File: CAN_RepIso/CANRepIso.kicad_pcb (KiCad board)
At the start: 4 copper layers, 57 x 27 mm, 82 parts, among them U1 SN74LV32ADGVR, U10 AP2205-33W5-7, U11 AP2205-33W5-7, U2 SN74LVC2G08DCUR, U3 SN74LVC2G07DBVR, U4 SN74LVC2G04DBVR, U5 SN74LVC2G132DCUR, U6 SN65HVD230, U7 PLACEHOLDER ISOLATOR, U8 SN65HVD230, U9 ADuM120N

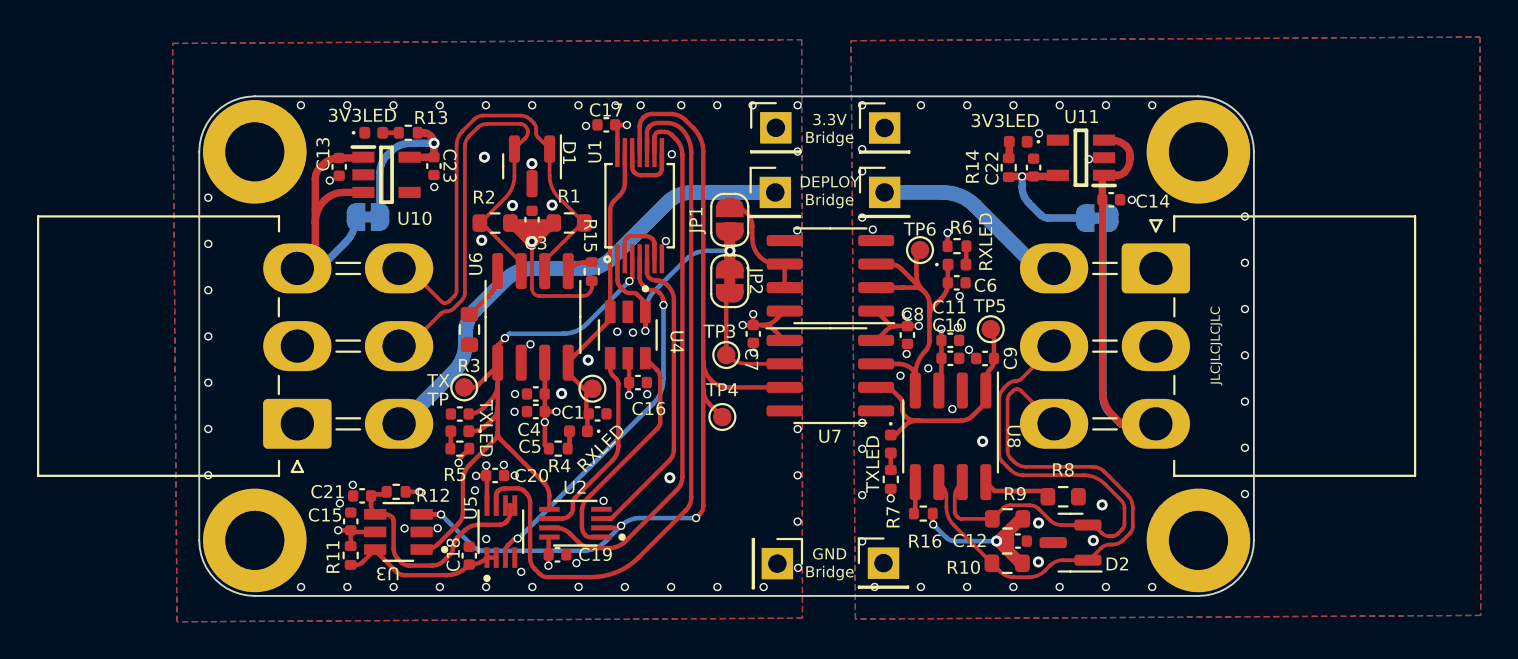
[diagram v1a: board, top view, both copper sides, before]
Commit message: clean up schematic and bom
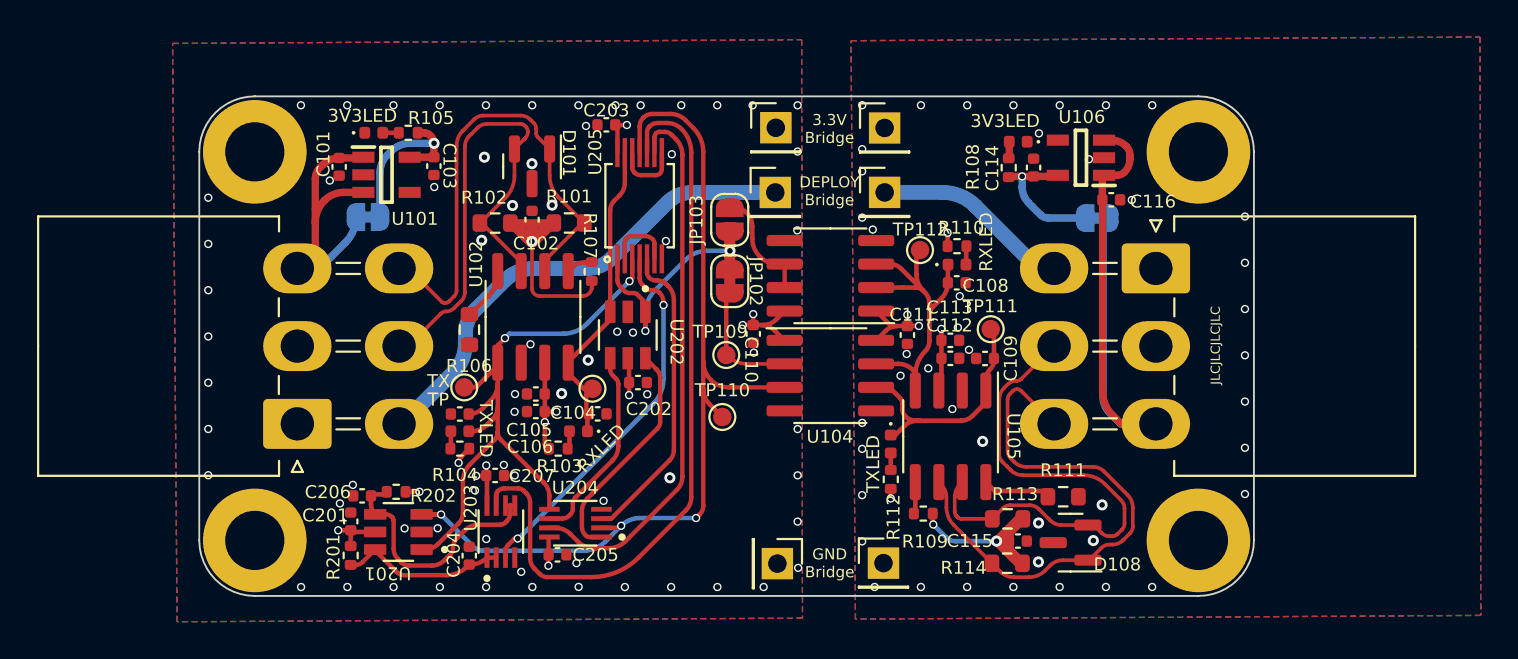
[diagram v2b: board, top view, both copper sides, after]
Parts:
- C201: renamed from C15; value 0.1uF -> 100nF
- C202: renamed from C16; value 0.1uF -> 100nF
- C203: renamed from C17; value 0.1uF -> 100nF
- C205: renamed from C19; value 0.1uF -> 100nF
- C207: renamed from C20; value 0.1uF -> 100nF
- D102: renamed from D3; value RX1LED -> LED_ORANGE
- D103: renamed from D4; value TX1LED -> LED_GREEN
- D104: renamed from D7; value 3V31LED -> LED_BLUE
- D105: renamed from D8; value 3V32LED -> LED_BLUE
- D106: renamed from D5; value RX2LED -> LED_ORANGE
- D107: renamed from D6; value TX2LED -> LED_GREEN
- renumbered C13 to C101, C3 to C102, C23 to C103, C1 to C104, C4 to C105, C5 to C106, C2 to C107, C6 to C108, C9 to C109, C7 to C110, C8 to C111, C10 to C112, C11 to C113, C22 to C114, C12 to C115, C14 to C116, C18 to C204, C21 to C206, D1 to D101, D2 to D108, H1 to H101, H2 to H102, H3 to H103, H4 to H104, RBUS1 to J101, RBUS2 to J102, JP4 to JP101, JP2 to JP102, JP1 to JP103, JP3 to JP104, R1 to R101, R2 to R102, R4 to R103, R5 to R104, R13 to R105, R3 to R106, R15 to R107, R14 to R108, R16 to R109, R6 to R110, R8 to R111, R7 to R112, R9 to R113, R10 to R114, R11 to R201, R12 to R202, TP1 to TP101, TP2 to TP102, TP11 to TP103, TP7 to TP104, TP8 to TP105, TP12 to TP106, TP9 to TP107, TP10 to TP108, TP3 to TP109, TP4 to TP110, TP5 to TP111, TP6 to TP112, U10 to U101, U6 to U102, U9 to U103, U7 to U104, U8 to U105, U11 to U106, U3 to U201, U4 to U202, U5 to U203, U2 to U204, U1 to U205
